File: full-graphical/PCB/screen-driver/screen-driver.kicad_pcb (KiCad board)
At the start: 2 copper layers, 139 x 139 mm, 170 parts, among them J1 Barrel_Jack_Switch, J10 Conn_01x05_Male, J2 ANODE - EVEN 2-60, J3 ANODE - EVEN-62-100, J4 CATHODE - EVEN - 42-100, J5 CATHODE ODD 41-99, J6 CATHODE EVEN 2-40, J7 CATHODE ODD 1-39, J8 ANODE - ODD 1-59, J9 ANODE - ODD 61-99, Q1 MPSA42, Q10 MPSA42, Q11 MPSA42, Q12 MPSA42, Q13 MPSA42, Q14 MPSA42, Q15 MPSA42, Q16 MPSA42, Q17 MPSA42, Q18 MPSA42, Q19 MPSA42, Q2 MPSA42, Q20 MPSA42, Q21 MPSA42, Q22 MPSA42, Q23 MPSA42, Q24 MPSA42, Q25 MPSA42, Q26 MPSA42, Q27 MPSA42, Q28 MPSA42, Q29 MPSA42, Q3 MPSA42, Q30 MPSA42, Q31 MPSA42, Q32 MPSA42, Q4 MPSA42, Q5 MPSA42, Q6 MPSA42, Q7 MPSA42, Q8 MPSA42, Q9 MPSA42, U1 SN755870, U2 ESP32-DEVKIT-V1, U3 SN755870, U4 TSR_1-2450, U5 CD4017BE, U6 CD4017BE

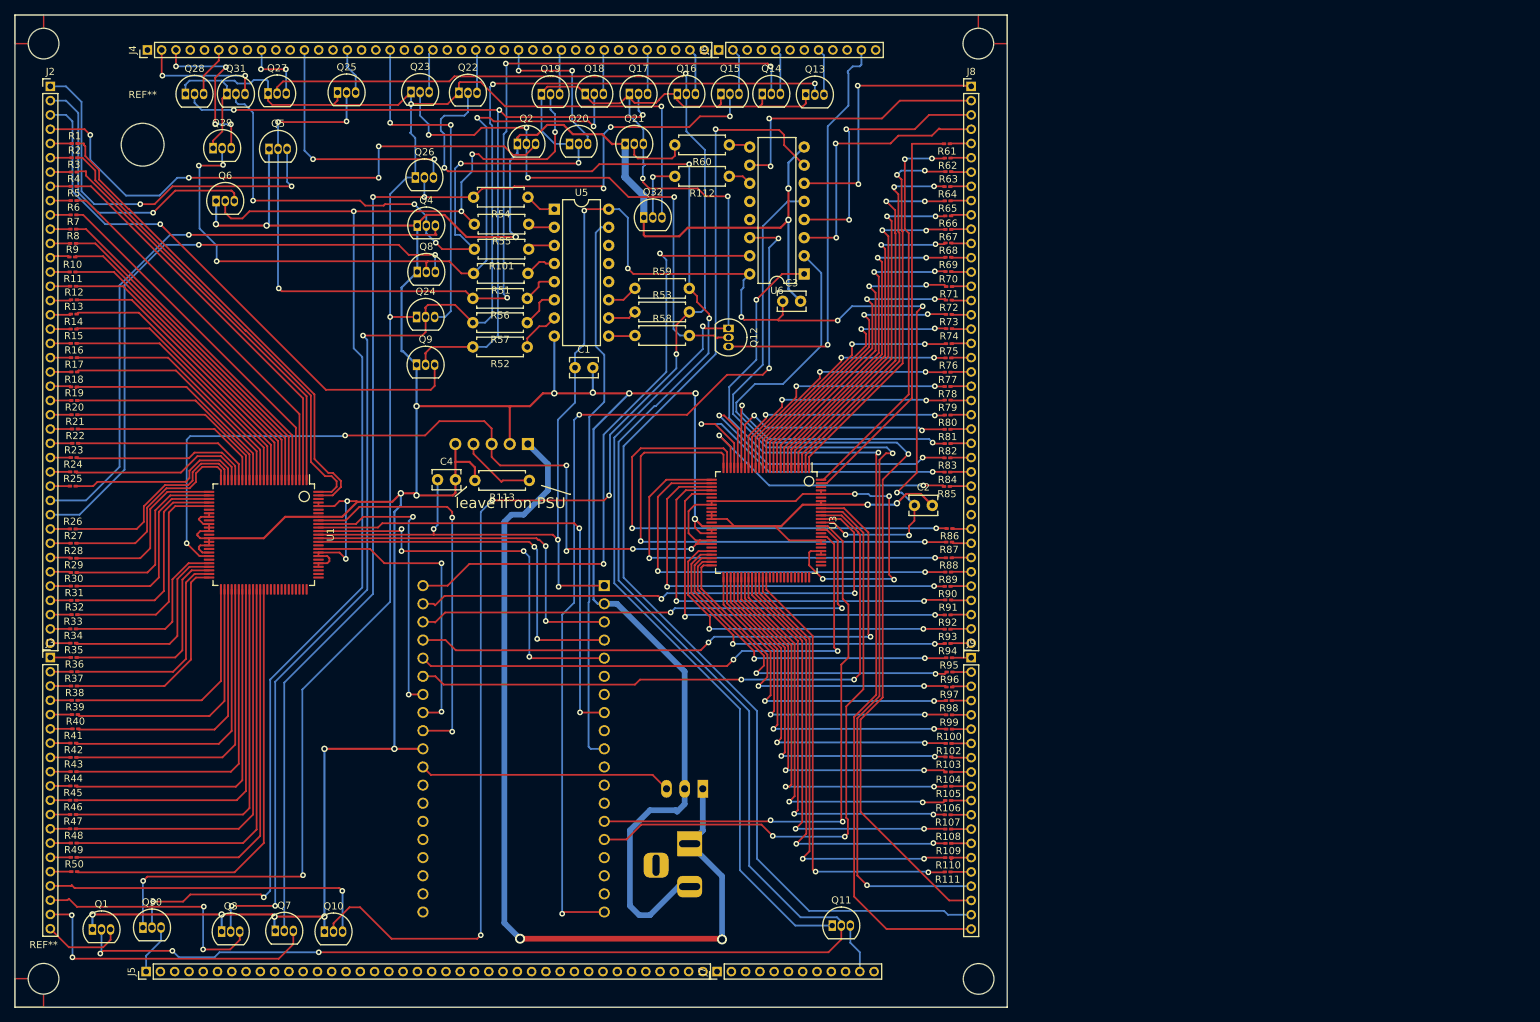
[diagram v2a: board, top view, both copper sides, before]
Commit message: fixed footprint error in pcb and improved ground traces
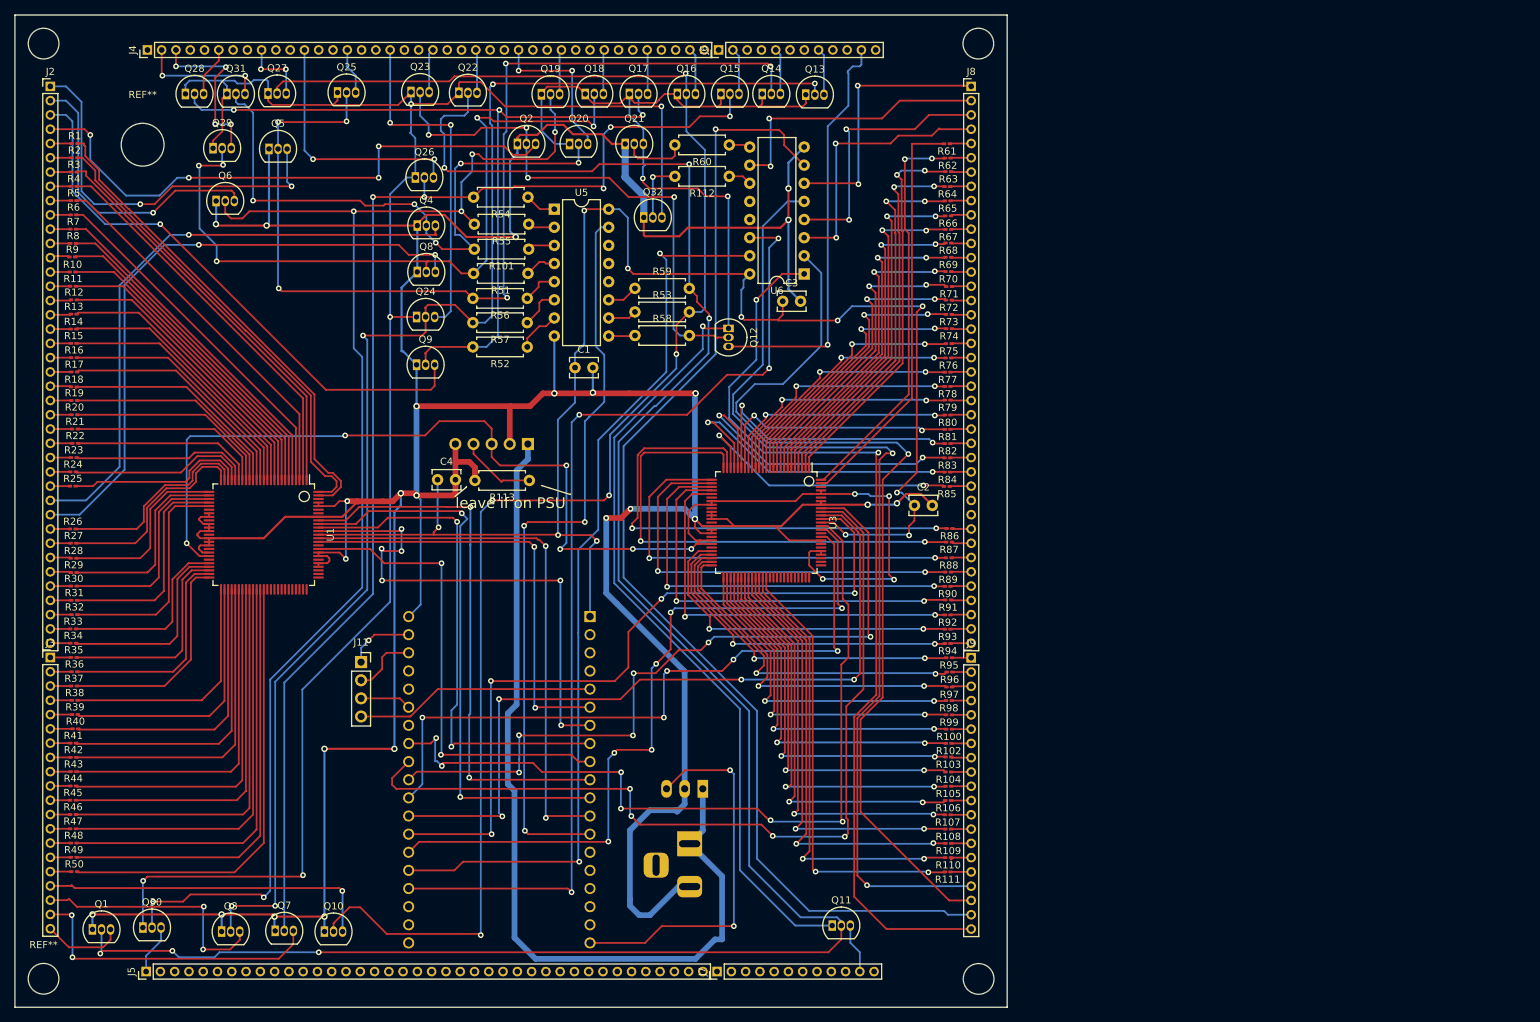
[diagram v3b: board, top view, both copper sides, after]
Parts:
- added J11: Conn_01x04, Connector_PinSocket_2.54mm:PinSocket_1x04_P2.54mm_Vertical, F.Cu at (134.8, 113.8)
- U2: value ESP32-DEVKIT-V1 -> ESP32-DEVKITC-32D
- moved U2 4.77 mm to (154.2, 127.2)
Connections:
- U2 pad 10: Net-(U2-Pad10) -> Net-(U1-Pad92)
- U2 pad 11: unconnected-(U2-Pad11) -> Net-(U1-Pad91)
- U2 pad 12: unconnected-(U2-Pad12) -> Net-(U1-Pad87)
- U2 pad 13: unconnected-(U2-Pad13) -> Net-(U5-Pad15)
- U2 pad 14: Net-(U2-Pad14) -> unconnected-(U2-Pad14)
- U2 pad 15: Net-(U2-Pad15) -> unconnected-(U2-Pad15)
- U2 pad 19: Net-(U2-Pad19) -> +5V
- U2 pad 2: GND -> unconnected-(U2-Pad2)
- U2 pad 20: Net-(U2-Pad20) -> GND
- U2 pad 23: Net-(U2-Pad23) -> unconnected-(U2-Pad23)
- U2 pad 24: Net-(U2-Pad24) -> unconnected-(U2-Pad24)
- U2 pad 26: Net-(U1-Pad91) -> unconnected-(U2-Pad26)
- U2 pad 27: Net-(U1-Pad84) -> Net-(U2-Pad27)
- U2 pad 28: Net-(U1-Pad92) -> Net-(U2-Pad28)
- U2 pad 29: GND -> Net-(U2-Pad29)
- U2 pad 3: Net-(U1-Pad87) -> unconnected-(U2-Pad3)
- U2 pad 30: +5V -> Net-(U2-Pad30)
- U2 pad 31: (no net) -> Net-(U2-Pad31)
- U2 pad 32: (no net) -> Net-(U2-Pad32)
- U2 pad 33: (no net) -> Net-(U2-Pad33)
- U2 pad 34: (no net) -> Net-(U2-Pad34)
- U2 pad 35: (no net) -> Net-(U2-Pad35)
- U2 pad 36: (no net) -> unconnected-(U2-Pad36)
- U2 pad 37: (no net) -> unconnected-(U2-Pad37)
- U2 pad 38: (no net) -> unconnected-(U2-Pad38)
- U2 pad 4: Net-(U1-Pad86) -> unconnected-(U2-Pad4)
- U2 pad 5: Net-(U1-Pad89) -> Net-(U2-Pad5)
- U2 pad 6: unconnected-(U2-Pad6) -> Net-(U1-Pad86)
- U2 pad 7: unconnected-(U2-Pad7) -> Net-(U1-Pad89)
- U2 pad 9: unconnected-(U2-Pad9) -> Net-(U1-Pad84)
- U3 pad 84: Net-(U2-Pad24) -> Net-(U2-Pad30)
- U3 pad 86: Net-(U2-Pad22) -> Net-(U2-Pad33)
- U3 pad 87: Net-(U2-Pad14) -> Net-(U2-Pad27)
- U3 pad 89: Net-(U2-Pad21) -> Net-(U2-Pad32)
- U3 pad 90: Net-(U2-Pad25) -> Net-(U2-Pad31)
- U3 pad 91: Net-(U2-Pad15) -> Net-(U2-Pad28)
- U3 pad 92: Net-(U2-Pad23) -> Net-(U2-Pad29)
- U5 pad 15: Net-(U2-Pad10) -> Net-(U5-Pad15)
- U6 pad 14: Net-(U2-Pad19) -> Net-(U2-Pad35)
- U6 pad 15: Net-(U2-Pad20) -> Net-(U2-Pad34)
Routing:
- net Net-(U2-Pad35): track 0.00 -> 142.5 mm, vias 0 -> 4
- net Net-(U2-Pad19): track 129.0 -> 0.00 mm, vias 4 -> 0
- net Net-(U2-Pad34): track 0.00 -> 127.9 mm, vias 0 -> 2
- net Net-(U2-Pad28): track 0.00 -> 123.7 mm, vias 0 -> 4
- net Net-(U2-Pad27): track 0.00 -> 115.9 mm, vias 0 -> 6
- net Net-(U2-Pad31): track 0.00 -> 107.9 mm, vias 0 -> 4
- net Net-(U2-Pad32): track 0.00 -> 106.1 mm, vias 0 -> 4
- net Net-(U5-Pad15): track 0.00 -> 105.1 mm, vias 0 -> 3
- net Net-(U2-Pad29): track 0.00 -> 104.1 mm, vias 0 -> 6
- net Net-(U2-Pad33): track 0.00 -> 104.1 mm, vias 0 -> 6
- net Net-(U2-Pad30): track 0.00 -> 95.1 mm, vias 0 -> 5
- net Net-(U2-Pad23): track 86.8 -> 0.00 mm, vias 2 -> 0
- net Net-(U2-Pad20): track 86.8 -> 0.00 mm, vias 2 -> 0
- net Net-(U2-Pad15): track 86.3 -> 0.00 mm, vias 2 -> 0
- net Net-(U2-Pad25): track 88.5 -> 7.18 mm, vias 2 -> 0
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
